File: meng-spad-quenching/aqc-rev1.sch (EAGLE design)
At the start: 137 parts, among them IC1 ADCMP582, IC2 NC7SV74K8X, IC3 LT3032-5, IC4 OPA342, IC5 OPA342, IC6 LTC1711, IC7 DS1100LU-20+, IC8 LT3032-15, IC9 NC7WZ16P6X, J1 VIN_LOGIC, M1 BSS806N, Q1 MMBTH81, Q2 MMBTH81, Q3 MMBTH81, Q4 MMBTH81, Q5 MMBTH81, Q6 MMBTH81, T1 MMBTH10, T2 MMBTH10, T3 MMBTH10, T4 MMBTH10, T5 MMBTH10, T6 MMBTH10, T7 MMBTH10, U1 SN65EPT21DGK, U2 TPS78233DDCT, U3 SN65EPT22DGK, X1 CONN_SPAD, X2 CONN_PHOTON_COUNTER, X3 CONN_FORCE_QUENCH, X4 CONN_VREF_ONE_SHOT_EXT, X5 CONN_VREF_DIAMOND_IBIAS_EXT, X6 CONN_VREF_CASCODE_IBIAS_EXT

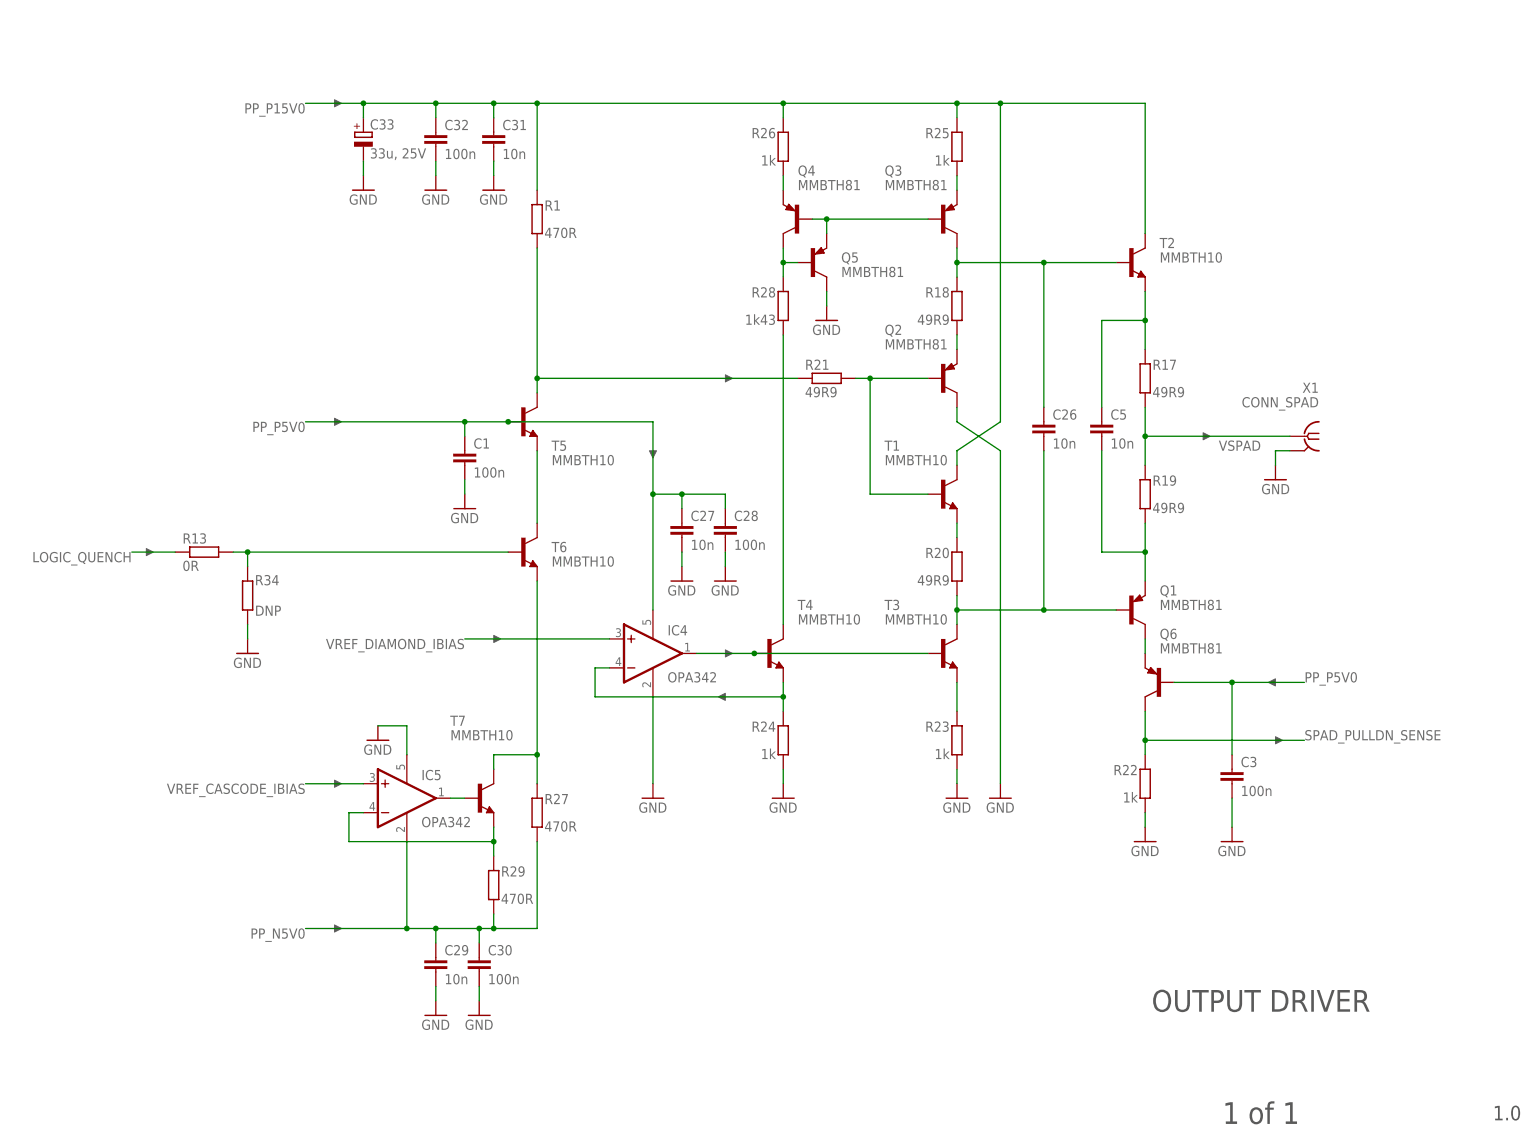
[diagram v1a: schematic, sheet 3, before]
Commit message: Switched low-voltage IC decoupling caps from 0603 to 0402
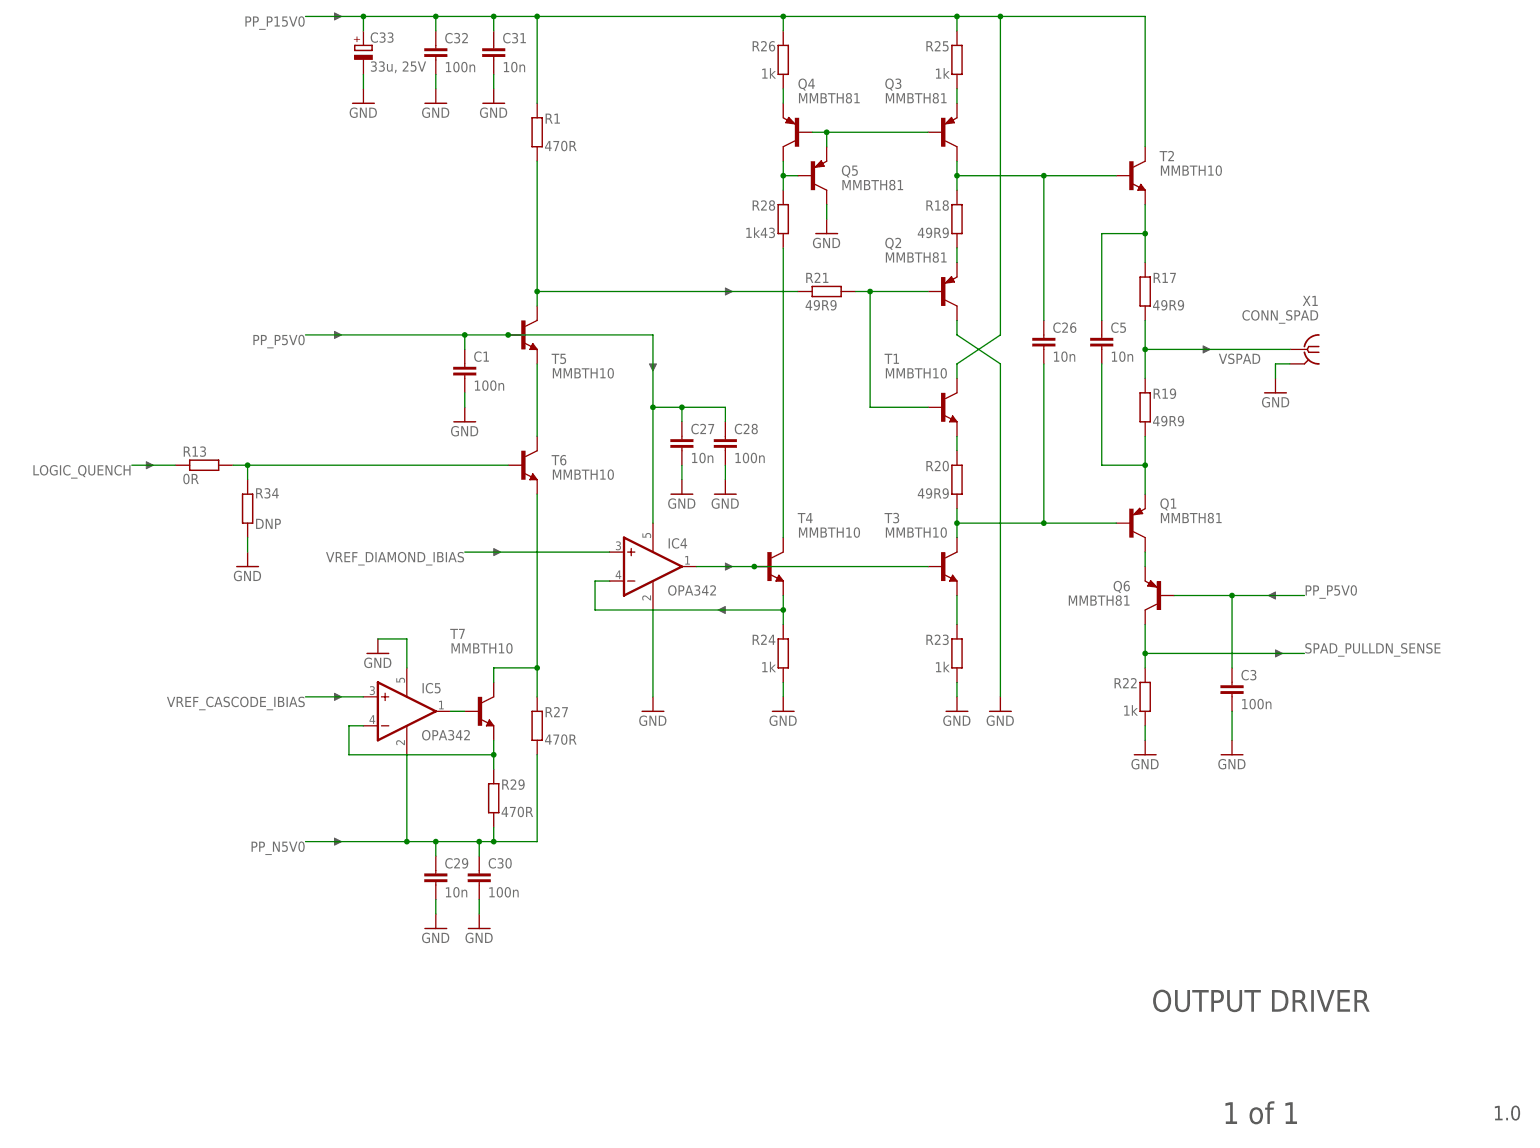
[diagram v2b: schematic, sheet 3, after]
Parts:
- C12, C13, C14, C15, C16, C17, C18, C19, C2, C22, C23, C24, C25, C27, C28, C29, C30, C34, C35, C36: device rcl:C-EUC0603 -> rcl:C-EUC0402
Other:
- moved on the sheet: C1, C26, C27, C28, C29, C3, C30, C31, C32, C33, C5, IC4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
